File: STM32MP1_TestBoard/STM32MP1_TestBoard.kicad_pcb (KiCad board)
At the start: 2 copper layers, 17.8 x 15.2 mm, 3 parts

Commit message: updated netlist
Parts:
- removed REF**: FBGA-78_7.5x11mm_Layout2x3x13_P0.8mm, Package_BGA:FBGA-78_7.5x11mm_Layout2x3x13_P0.8mm
- removed REF**: BGA-96_9.0x13.0mm_Layout2x3x16_P0.8mm, Package_BGA:BGA-96_9.0x13.0mm_Layout2x3x16_P0.8mm
- removed REF**: LFBGA-144_10x10mm_Layout12x12_P0.8mm, Package_BGA:LFBGA-144_10x10mm_Layout12x12_P0.8mm
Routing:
- net (no net): track 52.0 -> 0.00 mm, vias 5 -> 0
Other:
- board outline removed

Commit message: updated schematic design
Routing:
- added copper zone on In2.Cu_VDD, net +3V3
- added copper zone on In1.Cu_GND, net GNDS
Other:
- board outline added: 99.1 x 99.1 mm
- copper layers 2 -> 4
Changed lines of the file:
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@@
   (general
     (thickness 1.6)
-    (drawings 0)
+    (drawings 4)
     (tracks 0)
     (zones 0)
     (modules 0)
-    (nets 1)
+    (nets 3)
   )
   (page A4)
   (layers
-    (0 F.Cu signal)
-    (31 B.Cu signal)
+    (0 F.Cu_Signal signal)
+    (1 In1.Cu_GND power)
+    (2 In2.Cu_VDD power)
+    (31 B.Cu_Signal signal)
     (32 B.Adhes user)
     (33 F.Adhes user)
@@
     (46 B.CrtYd user)
     (47 F.CrtYd user)
-    (48 B.Fab user)
-    (49 F.Fab user)
+    (48 B.Fab user hide)
+    (49 F.Fab user hide)
   )
   (setup
@@
   )
   (net 0 "")
+  (net 1 GNDS)
+  (net 2 +3V3)
   (net_class Default "This is the default net class."
     (clearance 0.09)
@@
     (uvia_dia 0.3)
     (uvia_drill 0.1)
+    (add_net GNDS)
+  )
+  (gr_line (start 101.6 149.86) (end 101.6 50.8) (layer Edge.Cuts) (width 0.05))
+  (gr_line (start 200.66 149.86) (end 101.6 149.86) (layer Edge.Cuts) (width 0.05))
+  (gr_line (start 200.66 50.8) (end 200.66 149.86) (layer Edge.Cuts) (width 0.05))
+  (gr_line (start 101.6 50.8) (end 200.66 50.8) (layer Edge.Cuts) (width 0.05))
+  (zone (net 1) (net_name GNDS) (layer In1.Cu_GND) (hatch edge 0.508)
+    (connect_pads yes (clearance 0.508))
+    (min_thickness 0.254)
+    (fill yes (arc_segments 32) (thermal_gap 0.508) (thermal_bridge_width 0.508))
+    (polygon
+      (pts
+        (xy 200.66 149.86) (xy 101.6 149.86) (xy 101.6 50.8) (xy 200.66 50.8)
+      )
+    )
+  )
+  (zone (net 2) (net_name +3V3) (layer In2.Cu_VDD) (hatch edge 0.508)
+    (connect_pads yes (clearance 0.508))
+    (min_thickness 0.254)
+    (fill yes (arc_segments 32) (thermal_gap 0.508) (thermal_bridge_width 0.508))
+    (polygon
+      (pts
+        (xy 200.66 149.86) (xy 101.6 149.86) (xy 101.6 50.8) (xy 200.66 50.8)
+      )
+    )
   )
 )

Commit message: layout update
backup. work in progress
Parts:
- added C1: 1uF, Capacitor_SMD:C_0402_1005Metric_Pad0.74x0.62mm_HandSolder, F.Cu at (71.1, 78.0)
- added C10: 22uF, Capacitor_SMD:C_1206_3216Metric_Pad1.33x1.80mm_HandSolder, F.Cu at (60.3, 92.7)
- added C12: 1uF, Capacitor_SMD:C_0402_1005Metric_Pad0.74x0.62mm_HandSolder, B.Cu at (90.4, 93.0)
- added C13: 10nF, Capacitor_SMD:C_0402_1005Metric_Pad0.74x0.62mm_HandSolder, F.Cu at (124.9, 1.17)
- added C14: 1uF, Capacitor_SMD:C_0402_1005Metric_Pad0.74x0.62mm_HandSolder, B.Cu at (100.3, 101.1)
- added C15: 10nF, Capacitor_SMD:C_0402_1005Metric_Pad0.74x0.62mm_HandSolder, F.Cu at (124.9, 3.14)
- added C17: 1uF, Capacitor_SMD:C_0402_1005Metric_Pad0.74x0.62mm_HandSolder, B.Cu at (91.5, 104.4)
- added C18: 1uF, Capacitor_SMD:C_0402_1005Metric_Pad0.74x0.62mm_HandSolder, B.Cu at (87.2, 98.9)
- added C19: 1uF, Capacitor_SMD:C_0402_1005Metric_Pad0.74x0.62mm_HandSolder, B.Cu at (90.4, 100.9)
- added C2: 22uF, Capacitor_SMD:C_1206_3216Metric_Pad1.33x1.80mm_HandSolder, F.Cu at (64.8, 97.2)
- added C20: 1uF, Capacitor_SMD:C_0402_1005Metric_Pad0.74x0.62mm_HandSolder, B.Cu at (94.7, 104.4)
- added C21: 1uF, Capacitor_SMD:C_0402_1005Metric_Pad0.74x0.62mm_HandSolder, B.Cu at (87.2, 96.9)
- added C22: 1uF, Capacitor_SMD:C_0402_1005Metric_Pad0.74x0.62mm_HandSolder, B.Cu at (90.4, 98.9)
- added C23: 1uF, Capacitor_SMD:C_0402_1005Metric_Pad0.74x0.62mm_HandSolder, B.Cu at (93.6, 102.4)
- added C24: 1uF, Capacitor_SMD:C_0402_1005Metric_Pad0.74x0.62mm_HandSolder, B.Cu at (87.2, 95.0)
- added C25: 1uF, Capacitor_SMD:C_0402_1005Metric_Pad0.74x0.62mm_HandSolder, B.Cu at (97.9, 104.4)
- added C26: 1uF, Capacitor_SMD:C_0402_1005Metric_Pad0.74x0.62mm_HandSolder, B.Cu at (93.6, 100.5)
- added C27: 1uF, Capacitor_SMD:C_0402_1005Metric_Pad0.74x0.62mm_HandSolder, B.Cu at (90.4, 96.9)
- added C28: 1uF, Capacitor_SMD:C_0402_1005Metric_Pad0.74x0.62mm_HandSolder, B.Cu at (93.6, 94.6)
- added C29: 1uF, Capacitor_SMD:C_0402_1005Metric_Pad0.74x0.62mm_HandSolder, B.Cu at (87.2, 93.0)
- added C3: 10uF, Capacitor_SMD:C_0402_1005Metric_Pad0.74x0.62mm_HandSolder, F.Cu at (64.5, 77.7)
- added C30: 1uF, Capacitor_SMD:C_0402_1005Metric_Pad0.74x0.62mm_HandSolder, B.Cu at (96.8, 102.4)
- added C31: 1uF, Capacitor_SMD:C_0402_1005Metric_Pad0.74x0.62mm_HandSolder, B.Cu at (87.2, 100.9)
- added C32: 1uF, Capacitor_SMD:C_0402_1005Metric_Pad0.74x0.62mm_HandSolder, B.Cu at (90.4, 95.0)
- added C33: 1uF, Capacitor_SMD:C_0402_1005Metric_Pad0.74x0.62mm_HandSolder, B.Cu at (93.6, 98.5)
- added C34: 1uF, Capacitor_SMD:C_0402_1005Metric_Pad0.74x0.62mm_HandSolder, B.Cu at (96.8, 100.5)
- added C35: 1uF, Capacitor_SMD:C_0402_1005Metric_Pad0.74x0.62mm_HandSolder, B.Cu at (87.2, 91.0)
- added C36: 100nF, Capacitor_SMD:C_0402_1005Metric_Pad0.74x0.62mm_HandSolder, F.Cu at (236.2, 80.9)
- added C4: 100nF, Capacitor_SMD:C_0805_2012Metric_Pad1.18x1.45mm_HandSolder, F.Cu at (70.5, 93.3)
- added C40: 100nF, Capacitor_SMD:C_0402_1005Metric_Pad0.74x0.62mm_HandSolder, F.Cu at (220.9, 96.8)
- added C41: 100nF, Capacitor_SMD:C_0402_1005Metric_Pad0.74x0.62mm_HandSolder, F.Cu at (229.7, 86.8)
- added C42: 100nF, Capacitor_SMD:C_0402_1005Metric_Pad0.74x0.62mm_HandSolder, F.Cu at (223.2, 92.8)
- added C43: 100nF, Capacitor_SMD:C_0402_1005Metric_Pad0.74x0.62mm_HandSolder, F.Cu at (233.0, 82.9)
- added C44: 10uF, Capacitor_SMD:C_0402_1005Metric_Pad0.74x0.62mm_HandSolder, F.Cu at (217.7, 98.8)
- added C45: 10uF, Capacitor_SMD:C_0402_1005Metric_Pad0.74x0.62mm_HandSolder, F.Cu at (220.0, 94.8)
- added C46: 100nF, Capacitor_SMD:C_0402_1005Metric_Pad0.74x0.62mm_HandSolder, F.Cu at (226.5, 88.8)
- added C47: 100nF, Capacitor_SMD:C_0402_1005Metric_Pad0.74x0.62mm_HandSolder, F.Cu at (233.0, 80.9)
- added C48: 100nF, Capacitor_SMD:C_0402_1005Metric_Pad0.74x0.62mm_HandSolder, F.Cu at (223.2, 90.8)
- added C49: 100nF, Capacitor_SMD:C_0402_1005Metric_Pad0.74x0.62mm_HandSolder, F.Cu at (229.7, 84.8)
- added C5: 22uF, Capacitor_SMD:C_1206_3216Metric_Pad1.33x1.80mm_HandSolder, F.Cu at (62.2, 97.2)
- added C50: 100nF, Capacitor_SMD:C_0402_1005Metric_Pad0.74x0.62mm_HandSolder, F.Cu at (217.7, 96.8)
- added C51: 100nF, Capacitor_SMD:C_0402_1005Metric_Pad0.74x0.62mm_HandSolder, F.Cu at (220.9, 98.7)
- added C52: 100nF, Capacitor_SMD:C_0402_1005Metric_Pad0.74x0.62mm_HandSolder, F.Cu at (226.4, 94.7)
- added C53: 100nF, Capacitor_SMD:C_0402_1005Metric_Pad0.74x0.62mm_HandSolder, F.Cu at (220.0, 92.8)
- added C54: 100nF, Capacitor_SMD:C_0402_1005Metric_Pad0.74x0.62mm_HandSolder, F.Cu at (232.9, 88.8)
- added C55: 100nF, Capacitor_SMD:C_0402_1005Metric_Pad0.74x0.62mm_HandSolder, F.Cu at (236.1, 84.8)
- added C56: 100nF, Capacitor_SMD:C_0402_1005Metric_Pad0.74x0.62mm_HandSolder, F.Cu at (229.7, 90.8)
- added C57: 100nF, Capacitor_SMD:C_0402_1005Metric_Pad0.74x0.62mm_HandSolder, F.Cu at (224.1, 96.7)
- added C58: 100nF, Capacitor_SMD:C_0402_1005Metric_Pad0.74x0.62mm_HandSolder, F.Cu at (232.9, 86.8)
- added C59: 100nF, Capacitor_SMD:C_0402_1005Metric_Pad0.74x0.62mm_HandSolder, F.Cu at (226.4, 92.8)
- added C6: 56pF, Capacitor_SMD:C_0805_2012Metric_Pad1.18x1.45mm_HandSolder, F.Cu at (59.7, 97.0)
- added C60: 100nF, Capacitor_SMD:C_0402_1005Metric_Pad0.74x0.62mm_HandSolder, F.Cu at (236.2, 82.9)
- added C61: 100nF, Capacitor_SMD:C_0402_1005Metric_Pad0.74x0.62mm_HandSolder, F.Cu at (223.2, 94.8)
- added C62: 100nF, Capacitor_SMD:C_0402_1005Metric_Pad0.74x0.62mm_HandSolder, F.Cu at (229.7, 88.8)
- added C63: 100nF, Capacitor_SMD:C_0402_1005Metric_Pad0.74x0.62mm_HandSolder, F.Cu at (232.9, 84.8)
- added C64: 100nF, Capacitor_SMD:C_0402_1005Metric_Pad0.74x0.62mm_HandSolder, F.Cu at (229.7, 82.9)
- added C65: 100nF, Capacitor_SMD:C_0402_1005Metric_Pad0.74x0.62mm_HandSolder, F.Cu at (226.5, 86.9)
- added C66: 100nF, Capacitor_SMD:C_0402_1005Metric_Pad0.74x0.62mm_HandSolder, F.Cu at (226.5, 90.8)
- added C67: 100nF, Capacitor_SMD:C_0402_1005Metric_Pad0.74x0.62mm_HandSolder, F.Cu at (224.1, 98.7)
- added C68: 1uF, Capacitor_SMD:C_0402_1005Metric_Pad0.74x0.62mm_HandSolder, B.Cu at (93.6, 96.5)
- added C69: 2.2uF, Capacitor_SMD:C_0402_1005Metric_Pad0.74x0.62mm_HandSolder, B.Cu at (87.2, 89.0)
- added C7: 2.2uF, Capacitor_SMD:C_0402_1005Metric_Pad0.74x0.62mm_HandSolder, B.Cu at (90.4, 89.0)
- added C70: 1uF, Capacitor_SMD:C_0402_1005Metric_Pad0.74x0.62mm_HandSolder, B.Cu at (96.8, 98.5)
- added C8: 22uF, Capacitor_SMD:C_1206_3216Metric_Pad1.33x1.80mm_HandSolder, F.Cu at (60.3, 90.2)
- added C9: 2.2uF, Capacitor_SMD:C_0402_1005Metric_Pad0.74x0.62mm_HandSolder, B.Cu at (90.4, 91.0)
- added D1: LED, LED_SMD:LED_0805_2012Metric_Pad1.15x1.40mm_HandSolder, F.Cu at (139.2, 14.9)
- added J10: Conn_01x16, Connector_PinHeader_2.54mm:PinHeader_1x16_P2.54mm_Vertical, F.Cu at (121.9, 139.7)
- added J11: Conn_01x16, Connector_PinHeader_2.54mm:PinHeader_1x16_P2.54mm_Vertical, F.Cu at (119.4, 101.6)
- added J12: Micro_SD_Card, Molex_SDIO:Molex_SDIO_475710001, F.Cu at (160.0, 50.8)
- added J13: Micro_SD_Card, Molex_SDIO:Molex_SDIO_475710001, F.Cu at (180.6, 50.8)
- added J14: USB_B_Micro, Connector_USB:USB_Micro-B_Molex-105017-0001, F.Cu at (183.8, 146.1)
- added J15: USB_B, Connector_USB:USB_B_Lumberg_2411_02_Horizontal, F.Cu at (162.6, 134.1)
- added J2: Conn_02x05_Odd_Even, Connector_PinHeader_1.27mm:PinHeader_2x05_P1.27mm_Vertical_SMD, F.Cu at (169.4, 75.2)
- added J3: Conn_02x03_Odd_Even, Connector_PinHeader_2.54mm:PinHeader_2x03_P2.54mm_Vertical, F.Cu at (132.1, 11.0)
- added J4: Conn_01x16, Connector_PinHeader_2.54mm:PinHeader_1x16_P2.54mm_Vertical, F.Cu at (119.4, 99.1)
- added J5: Conn_01x06, Connector_PinHeader_2.54mm:PinHeader_1x06_P2.54mm_Vertical, F.Cu at (114.3, 91.4)
- added J6: Conn_01x16, Connector_PinHeader_2.54mm:PinHeader_1x16_P2.54mm_Vertical, F.Cu at (116.8, 61.0)
- added J7: Conn_01x16, Connector_PinHeader_2.54mm:PinHeader_1x16_P2.54mm_Vertical, F.Cu at (121.9, 61.0)
- added J8: Conn_01x12, Connector_PinHeader_2.54mm:PinHeader_1x12_P2.54mm_Vertical, F.Cu at (114.3, 61.0)
- added J9: Conn_01x06, Connector_PinHeader_2.54mm:PinHeader_1x06_P2.54mm_Vertical, F.Cu at (116.8, 101.6)
- added JP2: Jumper_NC_Small, Jumper:SolderJumper-2_P1.3mm_Bridged_Pad1.0x1.5mm, F.Cu at (161.5, 128.5)
- added JP3: Jumper_NC_Small, Jumper:SolderJumper-2_P1.3mm_Bridged_Pad1.0x1.5mm, F.Cu at (183.6, 136.4)
- added JP4: Jumper_NC_Small, Jumper:SolderJumper-2_P1.3mm_Bridged_Pad1.0x1.5mm, B.Cu at (87.7, 103.6)
- added JP5: Jumper_NC_Small, Jumper:SolderJumper-2_P1.3mm_Bridged_RoundedPad1.0x1.5mm, F.Cu at (122.0, 7.49)
- added JP6: Jumper_NC_Small, Jumper:SolderJumper-2_P1.3mm_Bridged_Pad1.0x1.5mm, F.Cu at (73.0, 93.3)
- added L2: 4.7uH, Inductor_SMD:L_Bourns-SRN6028, F.Cu at (54.0, 94.6)
- added L3: LQM18FN4R7M00D, Inductor_SMD:L_0201_0603Metric_Pad0.64x0.40mm_HandSolder, B.Cu at (93.6, 92.8)
- added Q1: DMG2302U, Package_TO_SOT_SMD:SOT-23, F.Cu at (67.1, 70.1)
- added R1: 1K, Resistor_SMD:R_0402_1005Metric_Pad0.72x0.64mm_HandSolder, F.Cu at (134.1, 19.4)
- added R10: 240R, Resistor_SMD:R_0402_1005Metric_Pad0.72x0.64mm_HandSolder, F.Cu at (220.0, 82.9)
- added R11: 240R, Resistor_SMD:R_0402_1005Metric_Pad0.72x0.64mm_HandSolder, F.Cu at (207.9, 96.9)
- added R12: 47K, Resistor_SMD:R_0402_1005Metric_Pad0.72x0.64mm_HandSolder, B.Cu at (156.8, 53.1)
- added R13: 47K, Resistor_SMD:R_0402_1005Metric_Pad0.72x0.64mm_HandSolder, B.Cu at (158.0, 53.1)
- added R14: 100R, Resistor_SMD:R_0402_1005Metric_Pad0.72x0.64mm_HandSolder, F.Cu at (216.7, 82.9)
- added R15: 10K, Resistor_SMD:R_0402_1005Metric_Pad0.72x0.64mm_HandSolder, F.Cu at (220.0, 80.9)
- added R16: 56R, Resistor_SMD:R_0402_1005Metric_Pad0.72x0.64mm_HandSolder, F.Cu at (204.7, 98.9)
- added R17: 56R, Resistor_SMD:R_0402_1005Metric_Pad0.72x0.64mm_HandSolder, F.Cu at (216.7, 80.9)
- added R18: 56R, Resistor_SMD:R_0402_1005Metric_Pad0.72x0.64mm_HandSolder, F.Cu at (214.4, 98.9)
- added R19: 56R, Resistor_SMD:R_0402_1005Metric_Pad0.72x0.64mm_HandSolder, F.Cu at (223.2, 86.9)
- added R2: 1K, Resistor_SMD:R_0402_1005Metric_Pad0.72x0.64mm_HandSolder, F.Cu at (223.2, 80.9)
- added R20: 56R, Resistor_SMD:R_0402_1005Metric_Pad0.72x0.64mm_HandSolder, F.Cu at (214.4, 96.9)
- added R21: 56R, Resistor_SMD:R_0402_1005Metric_Pad0.72x0.64mm_HandSolder, F.Cu at (226.5, 84.9)
- added R22: 56R, Resistor_SMD:R_0402_1005Metric_Pad0.72x0.64mm_HandSolder, F.Cu at (220.0, 90.8)
- added R23: 56R, Resistor_SMD:R_0402_1005Metric_Pad0.72x0.64mm_HandSolder, F.Cu at (229.7, 80.9)
- added R24: 56R, Resistor_SMD:R_0402_1005Metric_Pad0.72x0.64mm_HandSolder, F.Cu at (223.2, 88.9)
- added R25: 56R, Resistor_SMD:R_0402_1005Metric_Pad0.72x0.64mm_HandSolder, F.Cu at (216.7, 94.8)
- added R26: 56R, Resistor_SMD:R_0402_1005Metric_Pad0.72x0.64mm_HandSolder, F.Cu at (226.5, 82.9)
- added R27: 56R, Resistor_SMD:R_0402_1005Metric_Pad0.72x0.64mm_HandSolder, F.Cu at (211.2, 98.9)
- added R28: 56R, Resistor_SMD:R_0402_1005Metric_Pad0.72x0.64mm_HandSolder, F.Cu at (216.7, 92.8)
- added R29: 56R, Resistor_SMD:R_0402_1005Metric_Pad0.72x0.64mm_HandSolder, F.Cu at (216.7, 86.9)
- added R3: 100K, Resistor_SMD:R_0805_2012Metric_Pad1.20x1.40mm_HandSolder, F.Cu at (78.1, 97.2)
- added R30: 56R, Resistor_SMD:R_0402_1005Metric_Pad0.72x0.64mm_HandSolder, F.Cu at (216.7, 88.9)
- added R31: 56R, Resistor_SMD:R_0402_1005Metric_Pad0.72x0.64mm_HandSolder, F.Cu at (220.0, 84.9)
- added R32: 56R, Resistor_SMD:R_0402_1005Metric_Pad0.72x0.64mm_HandSolder, F.Cu at (204.7, 96.9)
- added R33: 56R, Resistor_SMD:R_0402_1005Metric_Pad0.72x0.64mm_HandSolder, F.Cu at (220.0, 86.9)
- added R34: 56R, Resistor_SMD:R_0402_1005Metric_Pad0.72x0.64mm_HandSolder, F.Cu at (223.2, 82.9)
- added R35: 56R, Resistor_SMD:R_0402_1005Metric_Pad0.72x0.64mm_HandSolder, F.Cu at (211.2, 96.9)
- added R36: 56R, Resistor_SMD:R_0402_1005Metric_Pad0.72x0.64mm_HandSolder, F.Cu at (223.2, 84.9)
- added R37: 56R, Resistor_SMD:R_0402_1005Metric_Pad0.72x0.64mm_HandSolder, F.Cu at (207.9, 98.9)
- added R38: 56R, Resistor_SMD:R_0402_1005Metric_Pad0.72x0.64mm_HandSolder, F.Cu at (216.7, 90.8)
- added R39: 56R, Resistor_SMD:R_0402_1005Metric_Pad0.72x0.64mm_HandSolder, F.Cu at (226.5, 80.9)
- added R4: 82K, Resistor_SMD:R_0805_2012Metric_Pad1.20x1.40mm_HandSolder, F.Cu at (75.6, 97.2)
- added R40: 47K, Resistor_SMD:R_0402_1005Metric_Pad0.72x0.64mm_HandSolder, B.Cu at (159.1, 53.1)
- added R41: 47K, Resistor_SMD:R_0402_1005Metric_Pad0.72x0.64mm_HandSolder, B.Cu at (163.4, 53.1)
- added R42: 47K, Resistor_SMD:R_0402_1005Metric_Pad0.72x0.64mm_HandSolder, B.Cu at (164.6, 53.1)
- added R43: 47K, Resistor_SMD:R_0402_1005Metric_Pad0.72x0.64mm_HandSolder, B.Cu at (177.4, 53.1)
- added R44: 47K, Resistor_SMD:R_0402_1005Metric_Pad0.72x0.64mm_HandSolder, B.Cu at (178.6, 53.1)
- added R45: 47K, Resistor_SMD:R_0402_1005Metric_Pad0.72x0.64mm_HandSolder, B.Cu at (179.7, 53.1)
- added R46: 47K, Resistor_SMD:R_0402_1005Metric_Pad0.72x0.64mm_HandSolder, B.Cu at (184.0, 53.1)
- added R47: 47K, Resistor_SMD:R_0402_1005Metric_Pad0.72x0.64mm_HandSolder, B.Cu at (185.2, 53.1)
- added R5: 1K, Resistor_SMD:R_0402_1005Metric_Pad0.72x0.64mm_HandSolder, F.Cu at (137.3, 19.4)
- added R52: 1K, Resistor_SMD:R_0402_1005Metric_Pad0.72x0.64mm_HandSolder, F.Cu at (220.0, 88.9)
- added R6: 10K, Resistor_SMD:R_0402_1005Metric_Pad0.72x0.64mm_HandSolder, F.Cu at (216.7, 84.9)
- added R7: 1K, Resistor_SMD:R_0402_1005Metric_Pad0.72x0.64mm_HandSolder, F.Cu at (131.4, 19.4)
- added R8: 3K, Resistor_SMD:R_0402_1005Metric_Pad0.72x0.64mm_HandSolder, F.Cu at (167.6, 102.4)
- added R9: 680R, Resistor_SMD:R_0402_1005Metric_Pad0.72x0.64mm_HandSolder, F.Cu at (142.5, 15.0)
- added SW2: SW_SPST, Button_Switch_SMD:Panasonic_EVQPUK_EVQPUB, F.Cu at (132.1, 5.08)
- added TP1: ~, TestPoint:TestPoint_Pad_D1.0mm, F.Cu at (227.2, 97.2)
- added TP2: ~, TestPoint:TestPoint_Pad_D1.0mm, F.Cu at (236.1, 87.3)
- added TP3: ~, TestPoint:TestPoint_Pad_D1.0mm, F.Cu at (229.6, 93.3)
- added U1: STM32MP157xAB, STM32MP151_LFBGA:BGA-361_19x19_16.0x16.0mm, F.Cu at (160.0, 90.1)
- added U2: MT41K256M16TW-107, Package_BGA:BGA-96_9.0x13.0mm_Layout2x3x16_P0.8mm, F.Cu at (188.7, 90.7)
- added U3: SE8233X2, Package_TO_SOT_SMD:SOT-23, F.Cu at (67.8, 77.5)
- added U4: TPS54202DDC, Package_TO_SOT_SMD:SOT-23-6, F.Cu at (68.6, 97.2)
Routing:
- net GNDS: track 0.00 -> 113.1 mm, vias 0 -> 65
- net /GPIO/SDMMC1_D0: track 0.00 -> 85.8 mm, vias 0 -> 2
- net Net-(J10-Pad7): track 0.00 -> 84.8 mm, vias 0 -> 1
- net /GPIO/SDMMC1_D2: track 0.00 -> 84.2 mm, vias 0 -> 4
- net /PSU/1.35V_VDDCORE: track 0.00 -> 78.6 mm, vias 0 -> 41
- net /GPIO/SDMMC1_CK: track 0.00 -> 73.4 mm, vias 0 -> 3
- net /GPIO/SDMMC1_D1: track 0.00 -> 72.8 mm, vias 0 -> 1
- net Net-(J10-Pad8): track 0.00 -> 72.2 mm
- net /GPIO/SDMMC1_D3: track 0.00 -> 72.2 mm, vias 0 -> 1
- net Net-(J10-Pad1): track 0.00 -> 66.6 mm, vias 0 -> 1
- net Net-(J10-Pad3): track 0.00 -> 59.4 mm
- net /GPIO/SDMMC2_CK: track 0.00 -> 59.4 mm
- net Net-(J10-Pad4): track 0.00 -> 58.2 mm, vias 0 -> 1
- net /GPIO/SDMMC2_D1: track 0.00 -> 58.0 mm, vias 0 -> 3
- net /DebugInterface1/3.3V_VDD: track 0.00 -> 55.1 mm, vias 0 -> 5
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- added copper zone on F.Cu, net +5V
- added copper zone on F.Cu, net /PSU/1.35V_VDDCORE
- added copper zone on In2.Cu_VDD_DDR, net /PSU/1.35V_VDDCORE
- added copper zone on F.Cu, net GNDS
- removed copper zone on In2.Cu_VDD, net +3V3

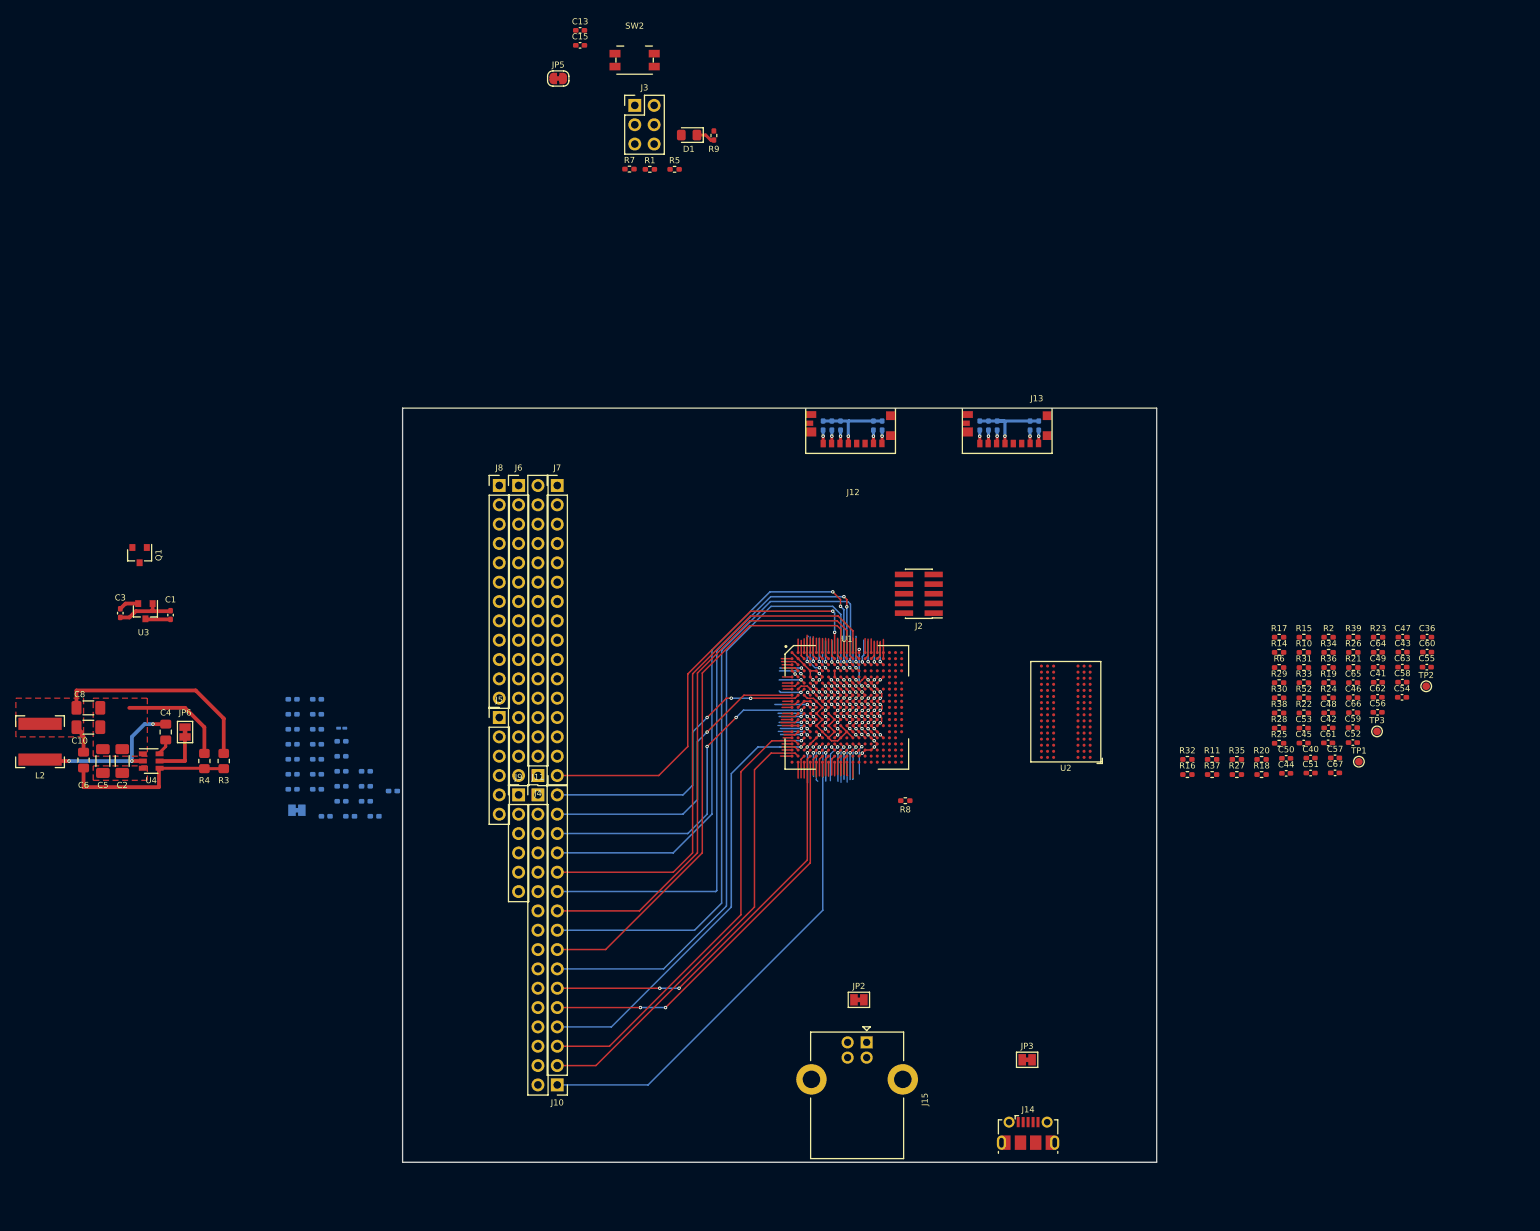
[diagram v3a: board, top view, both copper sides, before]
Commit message: added traces for sdio, dsi and swd connectors
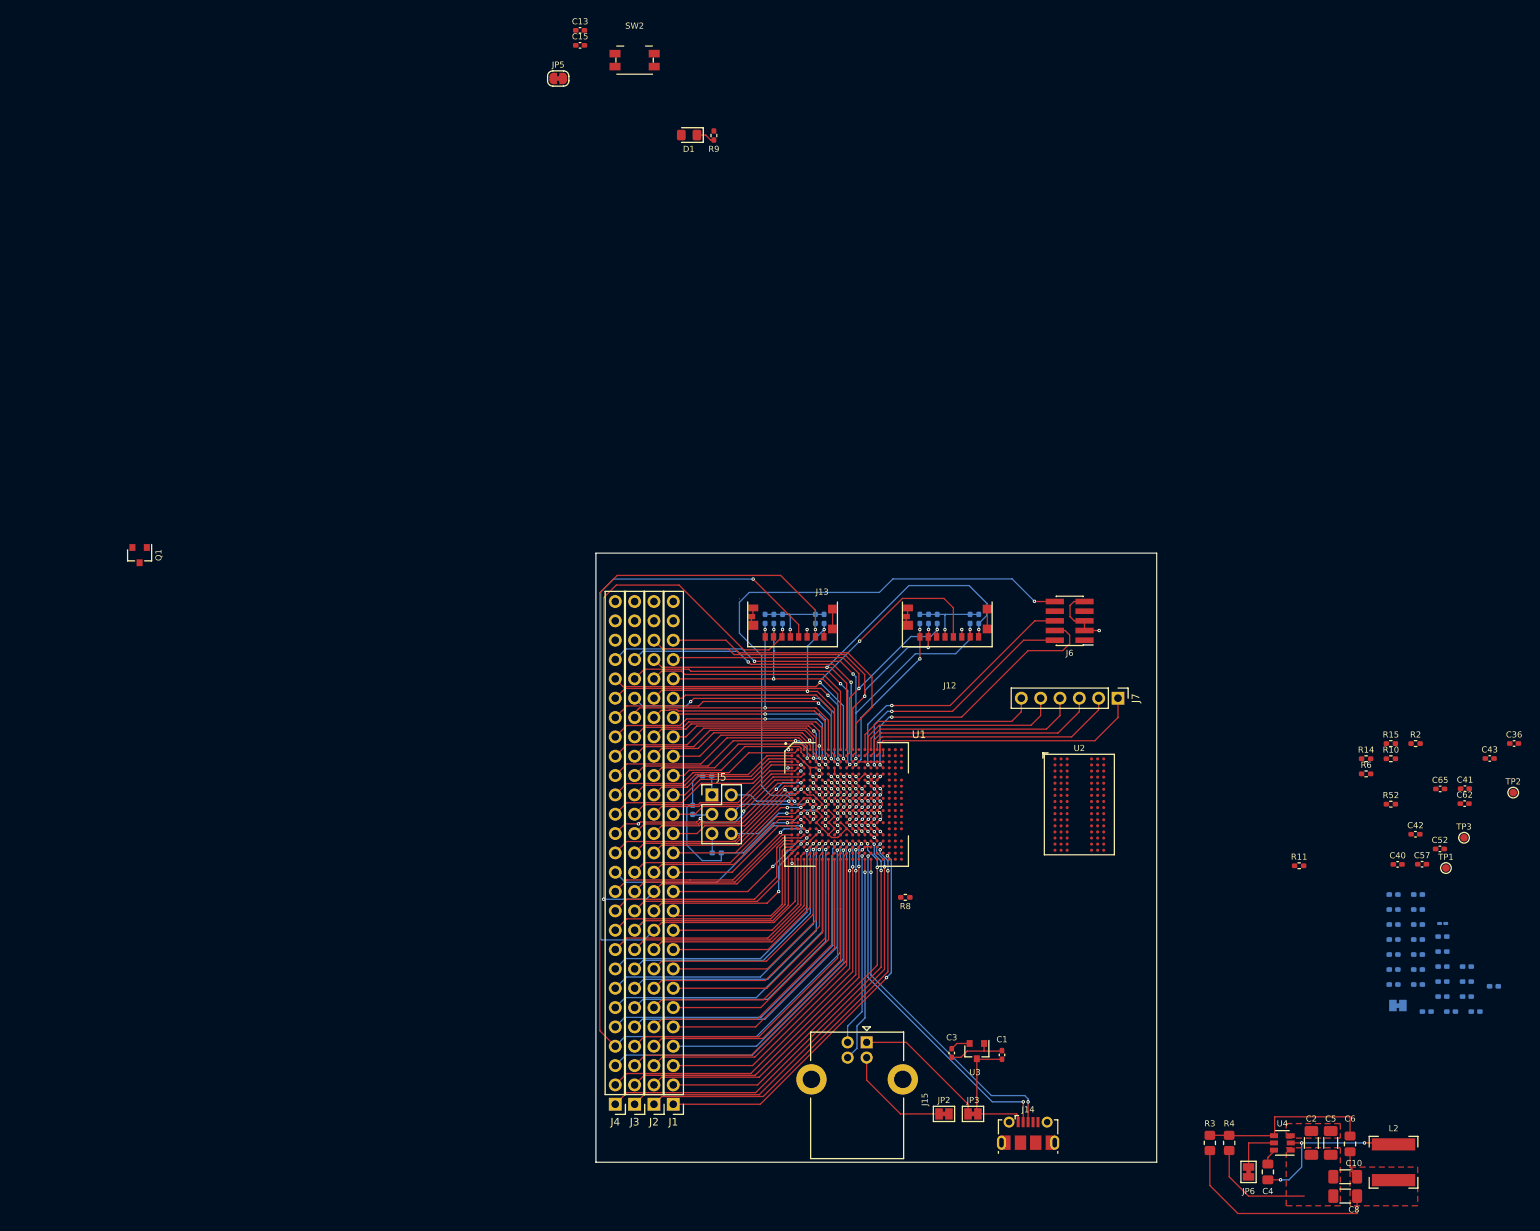
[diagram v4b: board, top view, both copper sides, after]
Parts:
- removed C44, C45: 10uF, Capacitor_SMD:C_0402_1005Metric_Pad0.74x0.62mm_HandSolder
- removed C46, C47, C48, C49, C50, C51, C53, C54, C55, C56, C58, C59, C60, C61, C63, C64, C66, C67: 100nF, Capacitor_SMD:C_0402_1005Metric_Pad0.74x0.62mm_HandSolder
- removed J10, J11: Conn_01x16, Connector_PinHeader_2.54mm:PinHeader_1x16_P2.54mm_Vertical
- removed the J6 at (116.8, 61.0)
- removed J8: Conn_01x12, Connector_PinHeader_2.54mm:PinHeader_1x12_P2.54mm_Vertical
- removed J9: Conn_01x06, Connector_PinHeader_2.54mm:PinHeader_1x06_P2.54mm_Vertical
- removed R16, R17, R18, R19, R20, R21, R22, R23, R24, R25, R26, R27, R28, R29, R30, R31, R32, R33, R34, R35, R36, R37, R38, R39: 56R, Resistor_SMD:R_0402_1005Metric_Pad0.72x0.64mm_HandSolder
- added J1: Conn_01x27, Connector_PinHeader_2.54mm:PinHeader_1x27_P2.54mm_Vertical, F.Cu at (137.2, 142.2)
- added J2: Conn_01x27, Connector_PinHeader_2.54mm:PinHeader_1x27_P2.54mm_Vertical, F.Cu at (134.6, 142.2)
- J3: value Conn_02x03_Odd_Even -> Conn_01x27; footprint Connector_PinHeader_2.54mm:PinHeader_2x03_P2.54mm_Vertical -> Connector_PinHeader_2.54mm:PinHeader_1x27_P2.54mm_Vertical
- J4: value Conn_01x16 -> Conn_01x27; footprint Connector_PinHeader_2.54mm:PinHeader_1x16_P2.54mm_Vertical -> Connector_PinHeader_2.54mm:PinHeader_1x27_P2.54mm_Vertical
- J5: value Conn_01x06 -> Conn_02x03_Odd_Even; footprint Connector_PinHeader_2.54mm:PinHeader_1x06_P2.54mm_Vertical -> Connector_PinHeader_2.54mm:PinHeader_2x03_P2.54mm_Vertical
- J7: value Conn_01x16 -> Conn_01x06; footprint Connector_PinHeader_2.54mm:PinHeader_1x16_P2.54mm_Vertical -> Connector_PinHeader_2.54mm:PinHeader_1x06_P2.54mm_Vertical
- R1, R5, R7: moved to B.Cu
- moved L2 186.2 mm to (231.8, 149.9), turned to 270 degrees
- moved C8 177.1 mm to (225.4, 154.3), turned to 180 degrees
- moved C10 175.3 mm to (225.4, 151.8), turned to 180 degrees
- moved C6 173.8 mm to (226.1, 147.4), turned to 270 degrees
- moved C5 168.9 mm to (223.5, 147.3), turned to 270 degrees
- moved C2 164.1 mm to (221.0, 147.3), turned to 270 degrees
- moved U4 156.8 mm to (217.2, 147.3), turned to 180 degrees
- moved C4 155.9 mm to (215.3, 151.1), turned to 90 degrees
- moved JP6 151.2 mm to (212.7, 151.1), turned to 90 degrees
- moved C14 146.9 mm to (245.0, 126.7)
- moved C23 146.9 mm to (238.2, 128.1)
- moved C26 146.9 mm to (238.2, 126.1)
- moved C28 146.9 mm to (238.2, 120.2)
- moved C33 146.9 mm to (238.2, 124.2)
- moved C68 146.9 mm to (238.2, 122.2)
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- renumbered J2 to J6
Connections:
- net /GPIO/SDMMC1_CMD renamed /GPIO/PD2
- net /GPIO/SDMMC1_D1 renamed /GPIO/PC9
- net /GPIO/SDMMC1_D3 renamed /GPIO/PC11
- net /GPIO/SDMMC2_CK renamed /GPIO/PC1
- net /GPIO/SDMMC2_CMD renamed /GPIO/PA0
- J12 pad 1: /GPIO/SDMMC1_D2 -> /GPIO/PC10
- J12 pad 5: /GPIO/SDMMC1_CK -> /GPIO/PC12
- J12 pad 7: /GPIO/SDMMC1_D0 -> /GPIO/PC8
- J13 pad 1: /GPIO/SDMMC2_D2 -> /GPIO/PB3
- J13 pad 2: /GPIO/SDMMC2_D3 -> /GPIO/PB4
- J13 pad 7: /GPIO/SDMMC2_D0 -> /GPIO/PB13
- J13 pad 8: /GPIO/SDMMC2_D1 -> /GPIO/PB15
- J3 pad 1: Net-(J3-Pad1) -> /GPIO/PA10
- J3 pad 2: Net-(J3-Pad2) -> /GPIO/PD13
- J3 pad 3: Net-(J3-Pad3) -> /GPIO/PE10
- J3 pad 4: Net-(J3-Pad4) -> /GPIO/PF6
- J3 pad 5: Net-(J3-Pad5) -> /GPIO/PF10
- J3 pad 6: Net-(J3-Pad6) -> /GPIO/PG8
- J4 pad 1: Net-(J4-Pad1) -> /GPIO/PG9
- J4 pad 10: Net-(J4-Pad10) -> /GPIO/PG13
- J4 pad 11: Net-(J4-Pad11) -> /GPIO/PE2
- J4 pad 12: Net-(J4-Pad12) -> /GPIO/PA5
- J4 pad 13: Net-(J4-Pad13) -> /GPIO/PA3
- J4 pad 14: Net-(J4-Pad14) -> /GPIO/PD9
- J4 pad 15: Net-(J4-Pad15) -> /GPIO/PG12
- J4 pad 16: Net-(J4-Pad16) -> /GPIO/PE14
- J4 pad 2: Net-(J4-Pad2) -> /GPIO/PE8
- J4 pad 3: Net-(J4-Pad3) -> /GPIO/PE7
- J4 pad 4: Net-(J4-Pad4) -> /GPIO/PB13
- J4 pad 5: Net-(J4-Pad5) -> /GPIO/PB5
- J4 pad 6: Net-(J4-Pad6) -> /GPIO/PC0
- J4 pad 7: Net-(J4-Pad7) -> /GPIO/PF11
- J4 pad 8: Net-(J4-Pad8) -> /GPIO/PA1
- J4 pad 9: Net-(J4-Pad9) -> /GPIO/PB1
- J7 pad 1: Net-(J7-Pad1) -> /GPIO/DSI_D1_P
- J7 pad 2: Net-(J7-Pad2) -> /GPIO/DSI_D1_N
- J7 pad 3: Net-(J7-Pad3) -> /GPIO/DSI_CK_P
- J7 pad 4: /GPIO/SDMMC2_D2 -> /GPIO/DSI_CK_N
- J7 pad 5: /GPIO/SDMMC2_D3 -> /GPIO/DSI_D0_P
- J7 pad 6: Net-(J7-Pad6) -> /GPIO/DSI_D0_N
- R1 pad 1: Net-(J3-Pad1) -> Net-(J5-Pad1)
- R12 pad 2: /GPIO/SDMMC1_D2 -> /GPIO/PC10
- R41 pad 2: /GPIO/SDMMC1_D0 -> /GPIO/PC8
- R43 pad 2: /GPIO/SDMMC2_D2 -> /GPIO/PB3
- R44 pad 2: /GPIO/SDMMC2_D3 -> /GPIO/PB4
- R46 pad 2: /GPIO/SDMMC2_D0 -> /GPIO/PB13
- R47 pad 2: /GPIO/SDMMC2_D1 -> /GPIO/PB15
- R5 pad 1: Net-(J3-Pad3) -> Net-(J5-Pad3)
- R7 pad 1: Net-(J3-Pad5) -> Net-(J5-Pad5)
- U1 pad A13: Net-(J9-Pad6) -> /GPIO/DSI_D0_N
- U1 pad A14: Net-(J9-Pad3) -> /GPIO/DSI_CK_N
- U1 pad A15: Net-(J9-Pad2) -> /GPIO/DSI_D1_N
- U1 pad A2: Net-(J8-Pad10) -> /GPIO/PG15
- U1 pad A3: Net-(J11-Pad1) -> /GPIO/PD0
- U1 pad A4: Net-(J11-Pad2) -> /GPIO/PD1
- U1 pad A5: Net-(J4-Pad4) -> /GPIO/PE3
- U1 pad A6: Net-(J8-Pad1) -> /GPIO/PG6
- U1 pad A7: /GPIO/SDMMC2_D2 -> /GPIO/PB3
- U1 pad A8: /GPIO/SDMMC2_D1 -> /GPIO/PB15
- U1 pad A9: Net-(J10-Pad8) -> /GPIO/PC7
- U1 pad B1: Net-(J4-Pad2) -> /GPIO/PE1
- U1 pad B11: Net-(J4-Pad5) -> /GPIO/PE4
- U1 pad B13: Net-(J9-Pad5) -> /GPIO/DSI_D0_P
- U1 pad B14: Net-(J9-Pad4) -> /GPIO/DSI_CK_P
- U1 pad B15: Net-(J9-Pad1) -> /GPIO/DSI_D1_P
- U1 pad B3: Net-(J4-Pad7) -> /GPIO/PE6
- U1 pad B4: Net-(J11-Pad8) -> /GPIO/PD7
- U1 pad B5: Net-(J7-Pad8) -> /GPIO/PB7
- U1 pad B7: Net-(J4-Pad6) -> /GPIO/PE5
- U1 pad B8: Net-(J6-Pad9) -> /GPIO/PA8
- U1 pad B9: /GPIO/SDMMC2_D3 -> /GPIO/PB4
- U1 pad C1: Net-(J4-Pad12) -> /GPIO/PE11
- U1 pad C10: /GPIO/SDMMC1_CK -> /GPIO/PC12
- U1 pad C11: /GPIO/SDMMC1_D0 -> /GPIO/PC8
- U1 pad C2: Net-(J4-Pad14) -> /GPIO/PE13
- U1 pad C4: Net-(J4-Pad1) -> /GPIO/PE0
- U1 pad C5: Net-(J11-Pad11) -> /GPIO/PD10
- U1 pad C6: Net-(J11-Pad4) -> /GPIO/PD3
- U1 pad C7: Net-(J6-Pad16) -> /GPIO/PA15
- U1 pad C8: Net-(J6-Pad10) -> /GPIO/PA9
- U1 pad C9: Net-(J7-Pad15) -> /GPIO/PB14
- U1 pad D10: Net-(J10-Pad7) -> /GPIO/PC6
- U1 pad D11: /GPIO/SDMMC1_D2 -> /GPIO/PC10
- U1 pad D2: Net-(J4-Pad13) -> /GPIO/PE12
- U1 pad D3: Net-(J4-Pad15) -> /GPIO/PE14
- U1 pad D6: Net-(J11-Pad5) -> /GPIO/PD4
- U1 pad D7: Net-(J11-Pad6) -> /GPIO/PD5
- U1 pad D9: Net-(J7-Pad10) -> /GPIO/PB9
- U1 pad E1: Net-(J4-Pad16) -> /GPIO/PE15
- U1 pad E3: Net-(J11-Pad7) -> /GPIO/PD6
- U1 pad F1: Net-(J8-Pad7) -> /GPIO/PG12
- U1 pad F2: Net-(J11-Pad9) -> /GPIO/PD8
- U1 pad F3: Net-(J11-Pad15) -> /GPIO/PD14
- U1 pad G1: Net-(J11-Pad16) -> /GPIO/PD15
- U1 pad G3: Net-(J11-Pad10) -> /GPIO/PD9
- U1 pad H1: Net-(J10-Pad15) -> /GPIO/PC14
- U1 pad H2: Net-(J10-Pad16) -> /GPIO/PC15
- U1 pad K1: Net-(J3-Pad2) -> Net-(J5-Pad2)
- U1 pad K3: Net-(J10-Pad14) -> /GPIO/PC13
- U1 pad K4: Net-(J3-Pad4) -> Net-(J5-Pad4)
- U1 pad L2: Net-(J3-Pad6) -> Net-(J5-Pad6)
- U1 pad M1: Net-(J8-Pad11) -> /GPIO/PH0
- U1 pad M2: Net-(J8-Pad12) -> /GPIO/PH1
- U1 pad P3: Net-(J6-Pad4) -> /GPIO/PA3
- U1 pad P4: Net-(J6-Pad6) -> /GPIO/PA5
- U1 pad R1: Net-(J6-Pad15) -> /GPIO/PA14
- U1 pad R4: Net-(J6-Pad5) -> /GPIO/PA4
- U1 pad T1: Net-(J4-Pad3) -> /GPIO/PE2
- U1 pad T10: Net-(J4-Pad8) -> /GPIO/PE7
- U1 pad T11: Net-(J4-Pad9) -> /GPIO/PE8
- U1 pad T12: Net-(J7-Pad7) -> /GPIO/PB6
- U1 pad T13: Net-(J7-Pad3) -> /GPIO/PB2
- U1 pad T14: Net-(J8-Pad4) -> /GPIO/PG9
- U1 pad T16: Net-(J6-Pad11) -> /GPIO/PA10
- U1 pad T2: Net-(J10-Pad3) -> /GPIO/PC2
- U1 pad T3: Net-(J10-Pad4) -> /GPIO/PC3
- U1 pad T5: Net-(J6-Pad7) (its old number) -> /GPIO/PA6
- U1 pad T6: Net-(J6-Pad8) (its old number) -> /GPIO/PA7
- U1 pad T7: Net-(J10-Pad1) -> /GPIO/PC0
- U1 pad T8: Net-(J7-Pad6) -> /GPIO/PB5
- U1 pad T9: /GPIO/SDMMC2_D0 -> /GPIO/PB13
- U1 pad U1: Net-(J8-Pad9) -> /GPIO/PG14
- U1 pad U10: Net-(J5-Pad3) -> /GPIO/PF8
- U1 pad U11: Net-(J11-Pad13) -> /GPIO/PD12
- U1 pad U12: Net-(J11-Pad14) -> /GPIO/PD13
- U1 pad U16: Net-(J6-Pad13) -> /GPIO/PA12
- U1 pad U2: Net-(J8-Pad8) -> /GPIO/PG13
- U1 pad U4: Net-(J6-Pad2) -> /GPIO/PA1
- U1 pad U5: Net-(J5-Pad6) -> /GPIO/PF11
- U1 pad U7: Net-(J8-Pad3) -> /GPIO/PG8
- U1 pad U9: Net-(J5-Pad5) -> /GPIO/PF10
- U1 pad V1: Net-(J7-Pad12) -> /GPIO/PB11
- U1 pad V10: Net-(J4-Pad11) -> /GPIO/PE10
- U1 pad V17: Net-(J6-Pad12) -> /GPIO/PA11
- U1 pad V3: Net-(J7-Pad2) -> /GPIO/PB1
- U1 pad V4: Net-(J10-Pad6) -> /GPIO/PC5
- U1 pad V5: Net-(J7-Pad13) -> /GPIO/PB12
- U1 pad V6: Net-(J8-Pad6) -> /GPIO/PG11
- U1 pad V7: Net-(J8-Pad5) -> /GPIO/PG10
- U1 pad V8: Net-(J11-Pad12) -> /GPIO/PD11
- U1 pad V9: Net-(J5-Pad1) -> /GPIO/PF6
- U1 pad W10: Net-(J8-Pad2) -> /GPIO/PG7
- U1 pad W2: Net-(J6-Pad3) -> /GPIO/PA2
- U1 pad W3: Net-(J7-Pad1) -> /GPIO/PB0
- U1 pad W4: Net-(J10-Pad5) -> /GPIO/PC4
- U1 pad W5: Net-(J7-Pad11) -> /GPIO/PB10
- U1 pad W6: Net-(J7-Pad9) -> /GPIO/PB8
- U1 pad W7: Net-(J4-Pad10) -> /GPIO/PE9
- U1 pad W8: Net-(J5-Pad2) -> /GPIO/PF7
- U1 pad W9: Net-(J5-Pad4) -> /GPIO/PF9
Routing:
- net /GPIO/PB13: track 0.00 -> 145.5 mm, vias 0 -> 2
- net /GPIO/PA0: track 5.06 -> 99.6 mm
- net /GPIO/SDMMC1_D0: track 85.8 -> 0.00 mm, vias 2 -> 0
- net Net-(J10-Pad7): track 84.8 -> 0.00 mm, vias 1 -> 0
- net /GPIO/SDMMC1_D2: track 84.2 -> 0.00 mm, vias 4 -> 0
- net /DebugInterface1/NRST: track 1.22 -> 75.0 mm, vias 0 -> 2
- net /GPIO/SDMMC1_CK: track 73.4 -> 0.00 mm, vias 3 -> 0
- net Net-(J10-Pad8): track 72.2 -> 0.00 mm
- net /GPIO/PC8: track 0.00 -> 67.1 mm, vias 0 -> 4
- net Net-(J10-Pad1): track 66.6 -> 0.00 mm, vias 1 -> 0
- net /GPIO/PC12: track 0.00 -> 66.0 mm, vias 0 -> 3
- net /GPIO/PC10: track 0.00 -> 64.3 mm, vias 0 -> 5
- net /GPIO/PG9: track 0.00 -> 59.5 mm, vias 0 -> 2
- net Net-(J10-Pad3): track 59.4 -> 0.00 mm
- net Net-(J10-Pad4): track 58.2 -> 0.00 mm, vias 1 -> 0
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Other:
- board size 99.1 x 99.1 mm -> 73.7 x 80 mm
